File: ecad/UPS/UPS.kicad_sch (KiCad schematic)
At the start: 0 parts

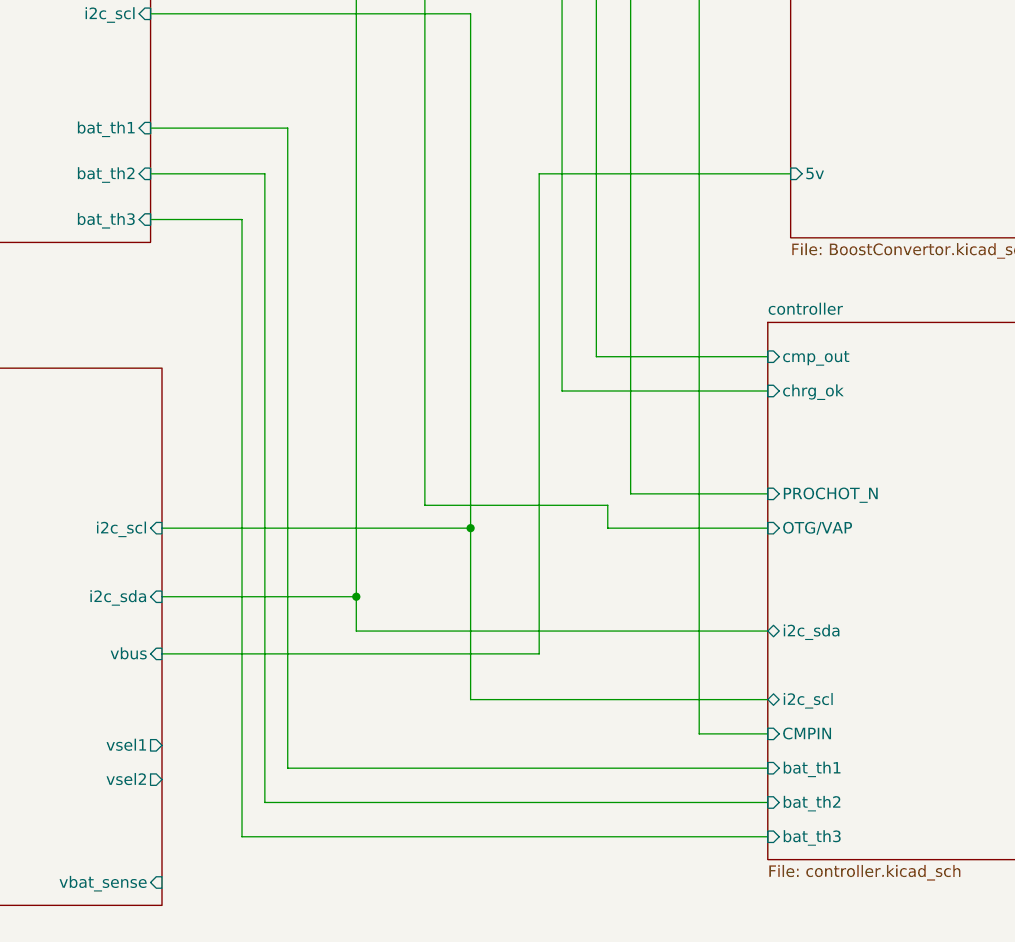
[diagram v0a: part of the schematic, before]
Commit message: Pins for thermistors, removed battery connector
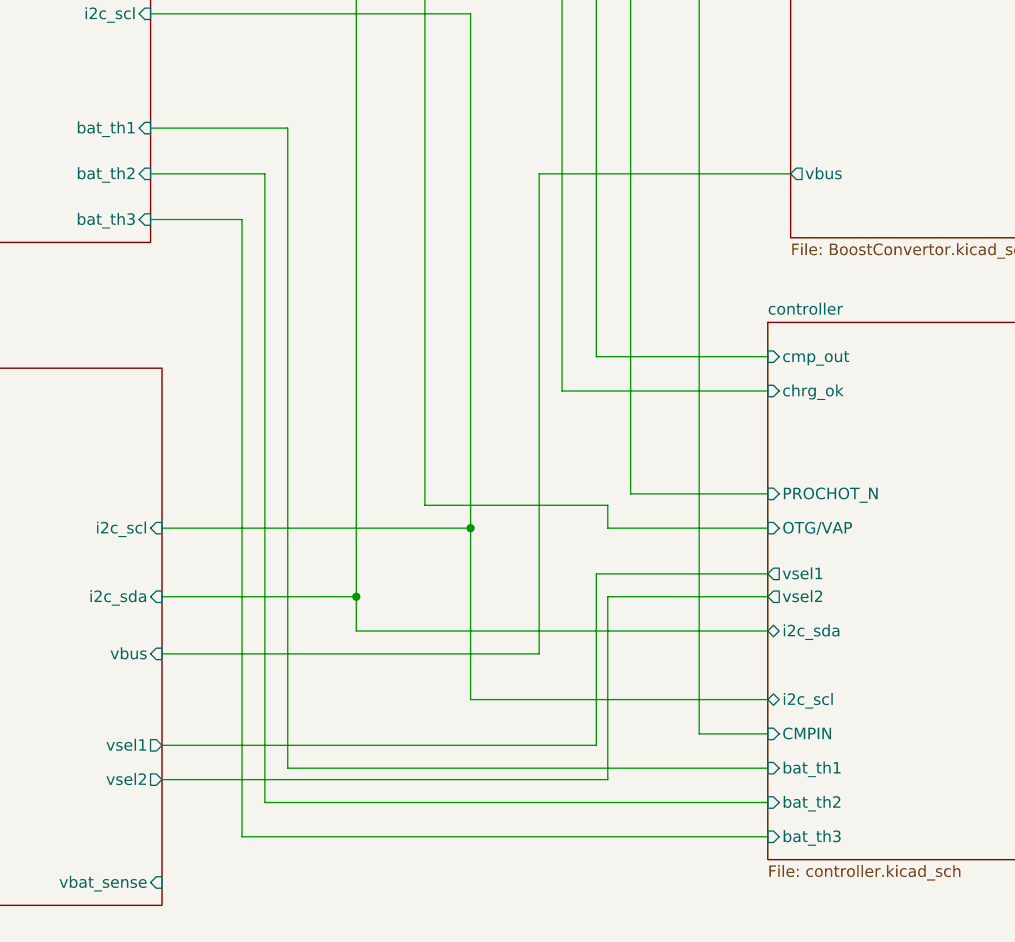
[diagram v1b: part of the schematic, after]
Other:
- sheet BoostConvertor ports: added vbus; removed 5v
- sheet controller ports: added vsel1, vsel2; removed none
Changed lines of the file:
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@@
 (kicad_sch
-	(version 20250114)
+	(version 20260306)
 	(generator "eeschema")
-	(generator_version "9.0")
+	(generator_version "10.0")
 	(paper "A4")
 	(title_block
@@
 	(wire
 		(pts
+			(xy 148.59 143.51) (xy 148.59 124.46)
+		)
+		(stroke
+			(width 0)
+			(type default)
+		)
+	)
+	(wire
+		(pts
+			(xy 149.86 127) (xy 149.86 147.32)
+		)
+		(stroke
+			(width 0)
+			(type default)
+		)
+	)
+	(wire
+		(pts
 			(xy 160.02 31.75) (xy 160.02 142.24)
 		)
@@
 	(wire
 		(pts
+			(xy 149.86 147.32) (xy 100.33 147.32)
+		)
+		(stroke
+			(width 0)
+			(type default)
+		)
+	)
+	(wire
+		(pts
 			(xy 121.92 130.81) (xy 121.92 127)
 		)
@@
 	(wire
 		(pts
+			(xy 148.59 124.46) (xy 167.64 124.46)
+		)
+		(stroke
+			(width 0)
+			(type default)
+		)
+	)
+	(wire
+		(pts
 			(xy 100.33 127) (xy 121.92 127)
 		)
@@
 	(wire
 		(pts
+			(xy 100.33 143.51) (xy 148.59 143.51)
+		)
+		(stroke
+			(width 0)
+			(type default)
+		)
+	)
+	(wire
+		(pts
 			(xy 99.06 80.01) (xy 111.76 80.01)
 		)
@@
 		(pts
 			(xy 109.22 85.09) (xy 109.22 153.67)
+		)
+		(stroke
+			(width 0)
+			(type default)
+		)
+	)
+	(wire
+		(pts
+			(xy 167.64 127) (xy 149.86 127)
 		)
 		(stroke
@@
 		)
 		(fill
-			(color 0 0 0 0.0000)
+			(color 0 0 0 0)
 		)
 		(property "Sheetname" "controller"
 			(at 167.64 95.8084 0)
+			(show_name no)
+			(do_not_autoplace no)
 			(effects
 				(font
@@
 		(property "Sheetfile" "controller.kicad_sch"
 			(at 167.64 156.7946 0)
+			(show_name no)
+			(do_not_autoplace no)
 			(effects
 				(font
@@
 		(property "Field2" ""
 			(at 167.64 96.52 0)
+			(show_name no)
+			(do_not_autoplace no)
 			(effects
 				(font
@@
 		(pin "i2c_sda" bidirectional
 			(at 167.64 130.81 180)
+			(effects
+				(font
+					(size 1.27 1.27)
+				)
+				(justify left)
+			)
+		)
+		(pin "vsel2" output
+			(at 167.64 127 180)
+			(effects
+				(font
+					(size 1.27 1.27)
+				)
+				(justify left)
+			)
+		)
+		(pin "vsel1" output
+			(at 167.64 124.46 180)
 			(effects
 				(font
@@
 		)
 		(fill
-			(color 0 0 0 0.0000)
+			(color 0 0 0 0)
 		)
 		(property "Sheetname" "Charger"
 			(at 25.4 25.9584 0)
+			(show_name no)
+			(do_not_autoplace no)
 			(effects
 				(font
@@
 		(property "Sheetfile" "Charger.kicad_sch"
 			(at 25.4 88.2146 0)
+			(show_name no)
+			(do_not_autoplace no)
 			(effects
 				(font
@@
 		)
 		(fill
-			(color 0 0 0 0.0000)
+			(color 0 0 0 0)
 		)
 		(property "Sheetname" "BoostConvertor"
 			(at 170.18 25.9584 0)
+			(show_name no)
+			(do_not_autoplace no)
 			(effects
 				(font
@@
 		(property "Sheetfile" "BoostConvertor.kicad_sch"
 			(at 170.18 87.7066 0)
+			(show_name no)
+			(do_not_autoplace no)
 			(effects
 				(font
@@
 			)
 		)
-		(pin "5v" input
+		(pin "vbus" output
 			(at 170.18 80.01 180)
 			(effects
@@
 		)
 		(fill
-			(color 0 0 0 0.0000)
+			(color 0 0 0 0)
 		)
 		(property "Sheetname" "Output"
 			(at 24.13 100.8884 0)
+			(show_name no)
+			(do_not_autoplace no)
 			(effects
 				(font
@@
 		(property "Sheetfile" "UPSOutput.kicad_sch"
 			(at 24.13 161.8746 0)
+			(show_name no)
+			(do_not_autoplace no)
 			(effects
 				(font
@@
 		(property "Field2" ""
 			(at 24.13 101.6 0)
-			(effects
-				(font
+			(show_name no)
+			(do_not_autoplace no)
+			(effects
+				(font
